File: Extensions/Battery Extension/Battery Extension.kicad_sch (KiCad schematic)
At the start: 23 parts, among them P4 Solder_Pad, U1 M1250RS-02P, U10 WJ126V-5_0-3P, U11 WJ126V-5_0-3P, U3 FS8205A, U4 TPS61032PWPR, U5 TP4056, U6 DW01A, U7 FXL0530-6R8-M, U8 AP40P05

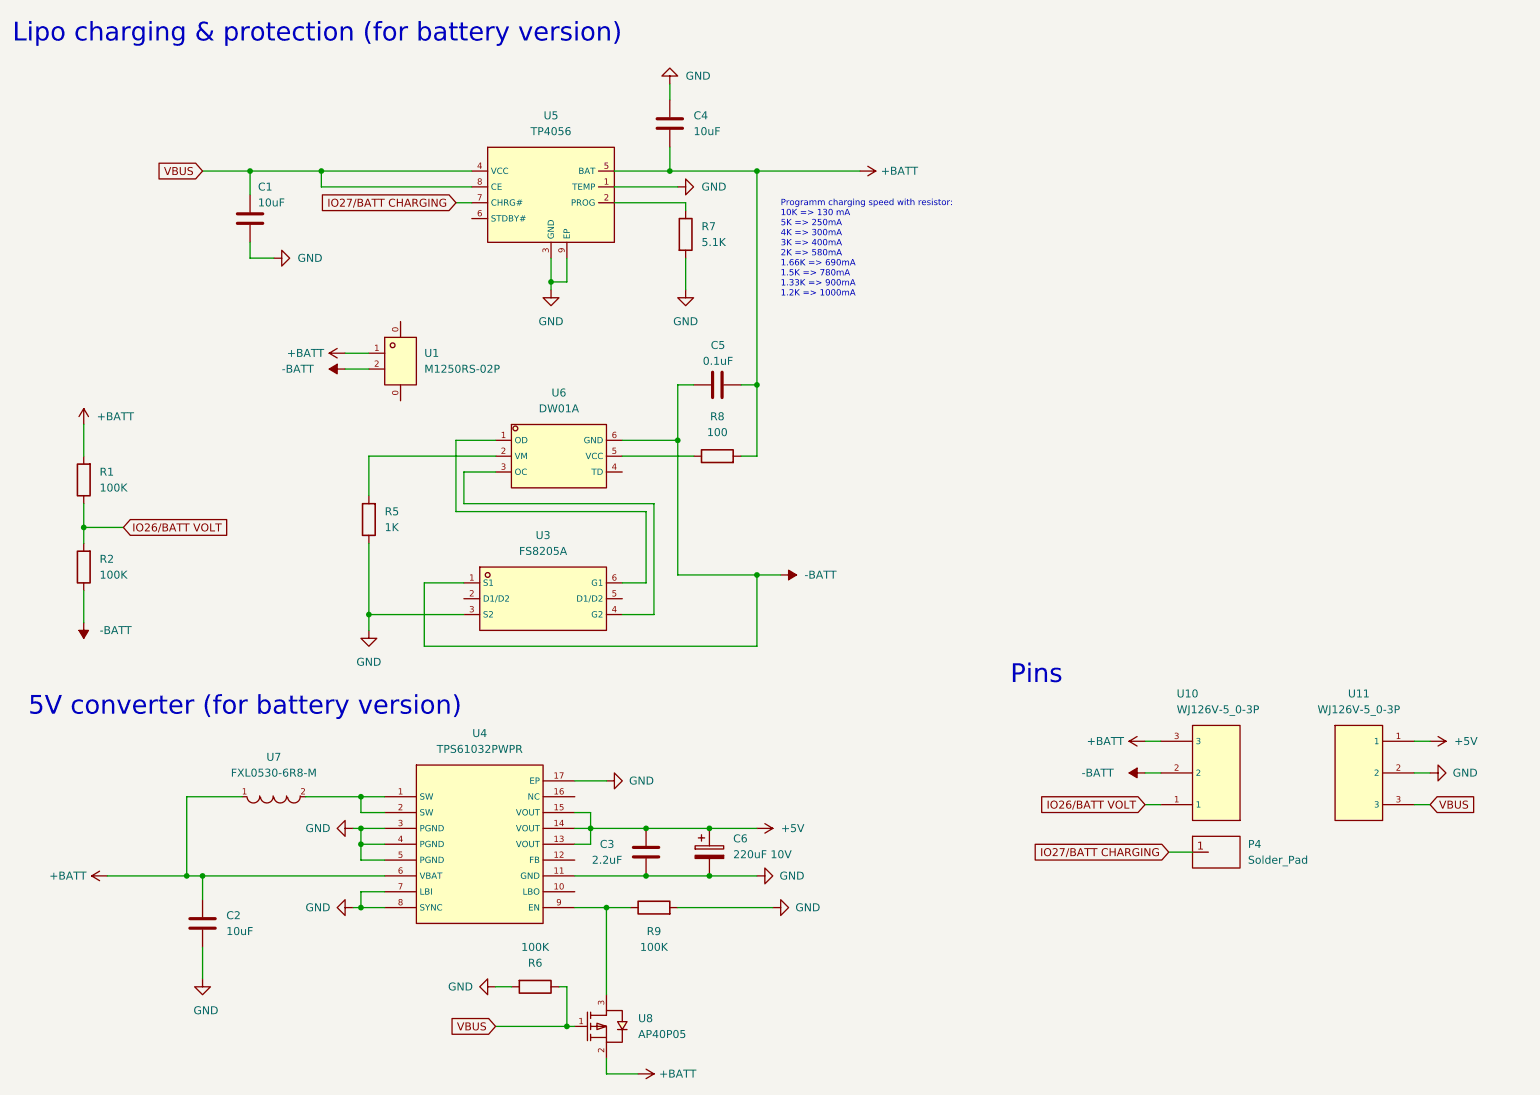
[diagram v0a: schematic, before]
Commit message: started replacing 0603 with 0402 caps and resistor
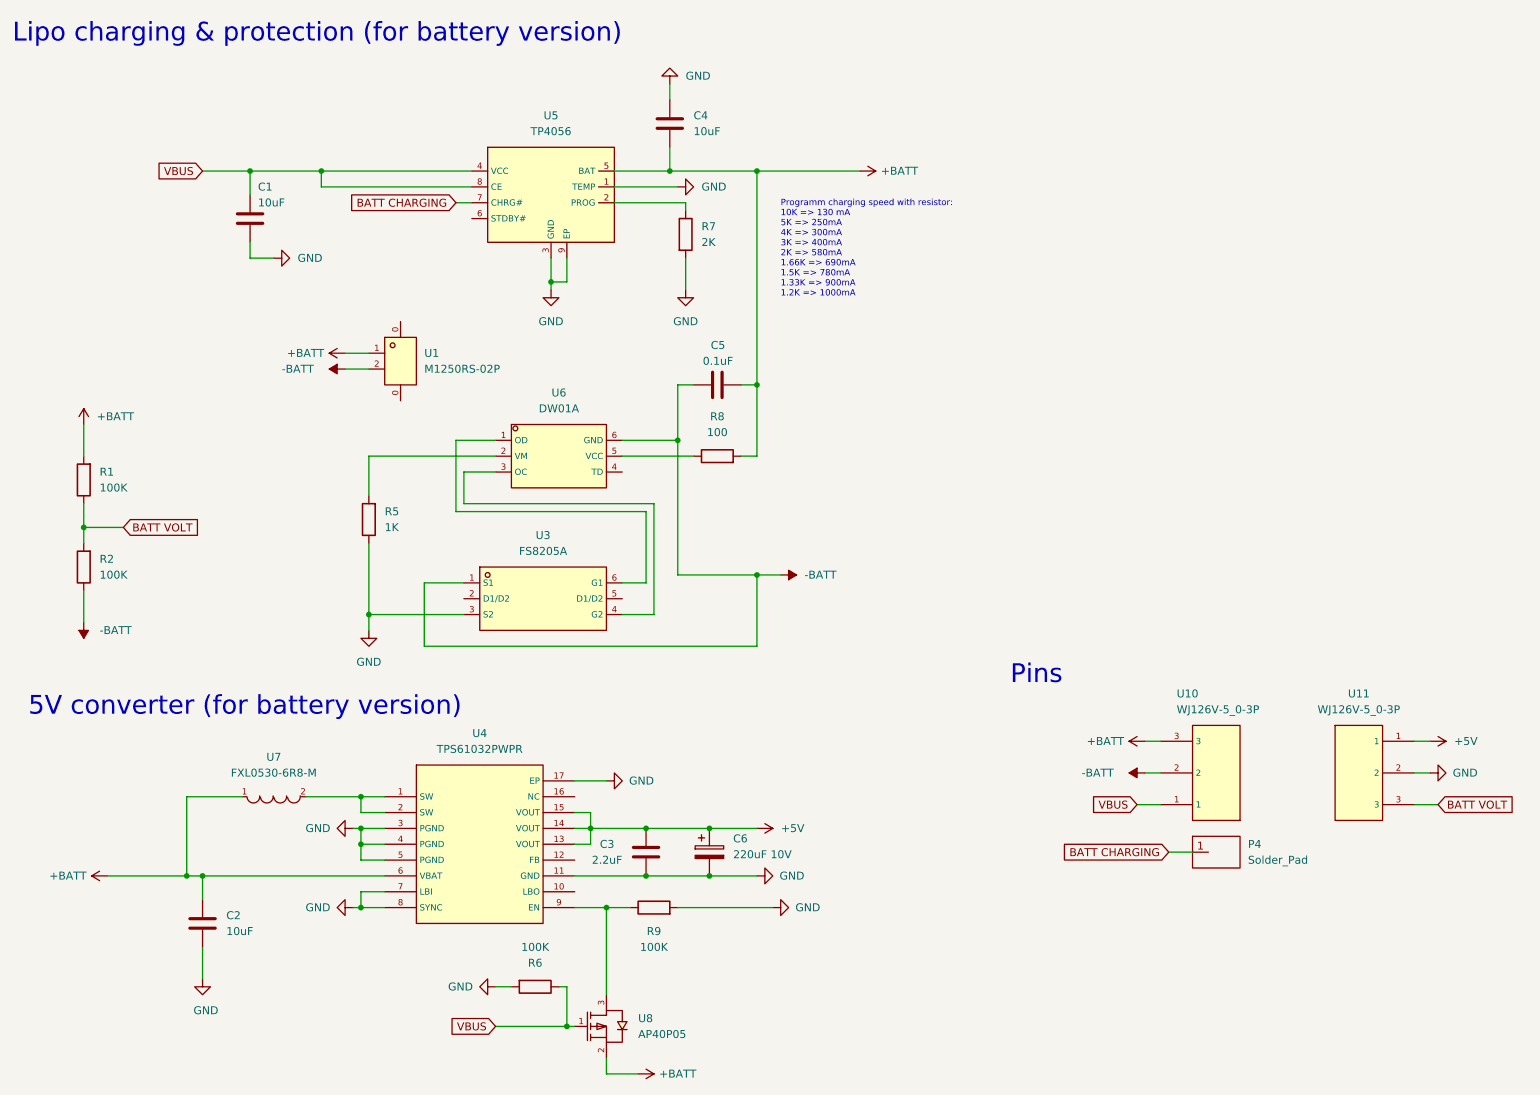
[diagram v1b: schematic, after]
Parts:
- C1, C2, C4: footprint Capacitor_SMD:C_0603_1608Metric_Pad1.08x0.95mm_HandSolder -> Capacitor_SMD:C_0603_1608Metric; LCSC # C19702 -> C96446
- C3: footprint Capacitor_SMD:C_0603_1608Metric_Pad1.08x0.95mm_HandSolder -> Capacitor_SMD:C_0603_1608Metric
- C5: footprint Capacitor_SMD:C_0603_1608Metric_Pad1.08x0.95mm_HandSolder -> Capacitor_SMD:C_0402_1005Metric; LCSC # C14663 -> C1525
- C6: LCSC # (none) -> C267466; LCSC Part # C267466 -> (none)
- R1, R2, R6, R9: footprint Resistor_SMD:R_0603_1608Metric_Pad0.98x0.95mm_HandSolder -> Resistor_SMD:R_0402_1005Metric; LCSC # C25803 -> C25741
- R5: footprint Resistor_SMD:R_0603_1608Metric_Pad0.98x0.95mm_HandSolder -> Resistor_SMD:R_0402_1005Metric; LCSC # C21190 -> C11702
- R7: value 5.1K -> 2K; footprint Resistor_SMD:R_0603_1608Metric_Pad0.98x0.95mm_HandSolder -> Resistor_SMD:R_0402_1005Metric; LCSC # C23186 -> C4109
- R8: footprint Resistor_SMD:R_0603_1608Metric_Pad0.98x0.95mm_HandSolder -> Resistor_SMD:R_0402_1005Metric; LCSC # C22775 -> C25076
- U10, U11: LCSC C8401 -> (none); LCSC # (none) -> C8401
- U4: LCSC C88716 -> (none); LCSC # (none) -> C88716
- U7: LCSC C177249 -> (none); LCSC # (none) -> C177249
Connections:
- net VBUS: now also U10.1; no longer U11.3
- net IO26/BATT VOLT renamed BATT VOLT
- net BATT VOLT: now also U11.3; no longer U10.1
- net IO27/BATT CHARGING renamed BATT CHARGING

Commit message: updated GlowCore PCB
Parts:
- R1: value 100K -> 33K; LCSC # C25741 -> C25779
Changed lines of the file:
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@@
       (effects (font (size 1.27 1.27)) (justify right))
     )
-    (property "Value" "100K" (id 1) (at 31.75 92.7099 0)
+    (property "Value" "33K" (id 1) (at 31.75 92.7099 0)
       (effects (font (size 1.27 1.27)) (justify right))
     )
@@
       (effects (font (size 1.27 1.27)) hide)
     )
-    (property "LCSC #" "C25741" (id 4) (at 29.21 91.44 0)
+    (property "LCSC #" "C25779" (id 4) (at 29.21 91.44 0)
       (effects (font (size 1.27 1.27)) hide)
     )
@@
     )
     (path "/06adb898-d256-45d2-b4ba-f50cc8c69bba"
-      (reference "R1") (unit 1) (value "100K") (footprint "Resistor_SMD:R_0402_1005Metric")
+      (reference "R1") (unit 1) (value "33K") (footprint "Resistor_SMD:R_0402_1005Metric")
     )
     (path "/69e62bb3-bcb6-44c6-b683-1c33658a3888"
